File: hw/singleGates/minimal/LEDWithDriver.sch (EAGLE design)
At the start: 8 parts, among them Q1 BC817, Q2 BC817, Q3 BC817

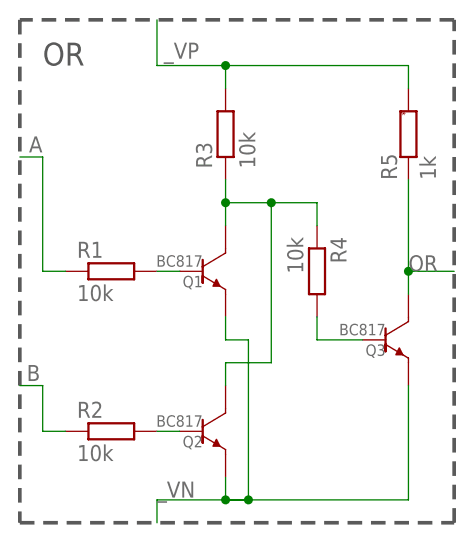
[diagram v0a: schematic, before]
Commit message: Add led output and prepare first alu slice
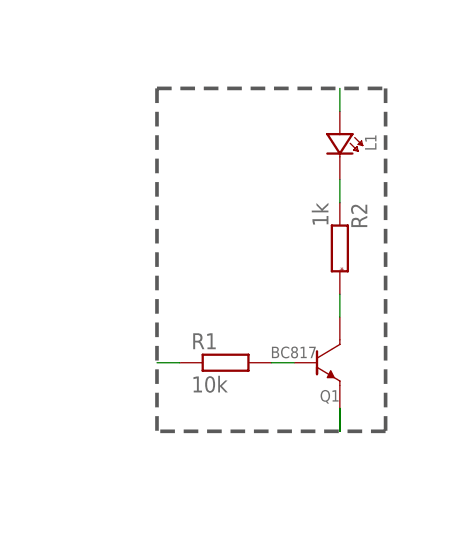
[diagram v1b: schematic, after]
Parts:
- removed Q2, Q3: BC817, p.peter-gator:TRANSISTOR-NPN-GENERICDEFAULT-SOT23-BEC
- removed R3, R4: 10k, p.peter-gator:R-EU_R0603
- removed R5: 1k, p.peter-rcl:R-EU-MARKEDR0603
- added L1: (no value), p.peter-leds:LED0603
- R2: value 10k -> 1k; device p.peter-gator:R-EU_R0603 -> p.peter-rcl:R-EU-MARKEDR0603
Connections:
- removed net B: R2.1
- removed net N$10: Q3.BASE, R4.2
- removed net N$11: Q1.COLLECTOR, Q2.COLLECTOR, R3.1, R4.1
- removed net N$9: Q2.BASE, R2.2
- removed net OR: Q3.COLLECTOR, R5.1
- new net INT: L1.C, R2.1
- new net N$1: Q1.COLLECTOR, R2.2
- net _VN: no longer Q2.EMITTER, Q3.EMITTER
- net _VP: now also L1.A; no longer R3.2, R5.2
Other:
- note removed: "OR"
- moved on the sheet: Q1, R1
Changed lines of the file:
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@@
 <parts>
 <part name="R1" library="p.peter-gator" deviceset="R-EU_" device="R0603" value="10k"/>
-<part name="R2" library="p.peter-gator" deviceset="R-EU_" device="R0603" value="10k"/>
-<part name="R3" library="p.peter-gator" deviceset="R-EU_" device="R0603" value="10k"/>
-<part name="R4" library="p.peter-gator" deviceset="R-EU_" device="R0603" value="10k"/>
-<part name="R5" library="p.peter-rcl" deviceset="R-EU-MARKED" device="R0603" value="1k"/>
+<part name="R2" library="p.peter-rcl" deviceset="R-EU-MARKED" device="R0603" value="1k"/>
 <part name="Q1" library="p.peter-gator" deviceset="TRANSISTOR-NPN-GENERIC" device="-SOT23-BEC" technology="DEFAULT" value="BC817"/>
-<part name="Q2" library="p.peter-gator" deviceset="TRANSISTOR-NPN-GENERIC" device="-SOT23-BEC" technology="DEFAULT" value="BC817"/>
-<part name="Q3" library="p.peter-gator" deviceset="TRANSISTOR-NPN-GENERIC" device="-SOT23-BEC" technology="DEFAULT" value="BC817"/>
+<part name="L1" library="p.peter-leds" deviceset="LED" device="0603"/>
 </parts>
 <sheets>
 <sheet>
 <plain>
-<wire x1="20.32" y1="-27.94" x2="20.32" y2="27.94" width="0.4064" layer="97" style="longdash"/>
-<wire x1="20.32" y1="27.94" x2="-27.94" y2="27.94" width="0.4064" layer="97" style="longdash"/>
-<wire x1="-27.94" y1="27.94" x2="-27.94" y2="-27.94" width="0.4064" layer="97" style="longdash"/>
-<wire x1="-27.94" y1="-27.94" x2="20.32" y2="-27.94" width="0.4064" layer="97" style="longdash"/>
-<text x="-25.4" y="22.86" size="2.54" layer="97" ratio="12">OR</text>
+<wire x1="12.7" y1="-17.78" x2="-12.7" y2="-17.78" width="0.4064" layer="97" style="longdash"/>
+<wire x1="-12.7" y1="20.32" x2="-12.7" y2="-17.78" width="0.4064" layer="97" style="longdash"/>
+<wire x1="12.7" y1="20.32" x2="12.7" y2="-17.78" width="0.4064" layer="97" style="longdash"/>
+<wire x1="-12.7" y1="20.32" x2="12.7" y2="20.32" width="0.4064" layer="97" style="longdash"/>
 </plain>
 <instances>
-<instance part="R1" gate="G$1" x="-17.78" y="0"/>
-<instance part="R2" gate="G$1" x="-17.78" y="-17.78"/>
-<instance part="R3" gate="G$1" x="-5.08" y="15.24" rot="R90"/>
-<instance part="R4" gate="G$1" x="5.08" y="0" rot="R270"/>
-<instance part="R5" gate="G$1" x="15.24" y="15.24" rot="R90"/>
-<instance part="Q1" gate="G$1" x="-5.08" y="0" smashed="yes">
-<attribute name="NAME" x="-7.62" y="-1.778" size="1.27" layer="95" ratio="12" rot="R180" align="top-left"/>
-<attribute name="VALUE" x="-7.62" y="1.778" size="1.27" layer="96" ratio="12" rot="R180"/>
+<instance part="R1" gate="G$1" x="-5.08" y="-10.16"/>
+<instance part="R2" gate="G$1" x="7.62" y="2.54" rot="R270"/>
+<instance part="Q1" gate="G$1" x="7.62" y="-10.16" smashed="yes">
+<attribute name="NAME" x="7.62" y="-14.478" size="1.27" layer="95" ratio="12" rot="R180" align="top-left"/>
+<attribute name="VALUE" x="5.08" y="-8.382" size="1.27" layer="96" ratio="12" rot="R180"/>
 </instance>
-<instance part="Q2" gate="G$1" x="-5.08" y="-17.78" smashed="yes">
-<attribute name="NAME" x="-7.62" y="-19.558" size="1.27" layer="95" ratio="12" rot="R180" align="top-left"/>
-<attribute name="VALUE" x="-7.62" y="-16.002" size="1.27" layer="96" ratio="12" rot="R180"/>
-</instance>
-<instance part="Q3" gate="G$1" x="15.24" y="-7.62" smashed="yes">
-<attribute name="NAME" x="12.7" y="-9.398" size="1.27" layer="95" ratio="12" rot="R180" align="top-left"/>
-<attribute name="VALUE" x="12.7" y="-5.842" size="1.27" layer="96" ratio="12" rot="R180"/>
-</instance>
+<instance part="L1" gate="G$1" x="7.62" y="15.24" rot="R270"/>
 </instances>
 <busses>
 </busses>
 <nets>
+<net name="_VN" class="0">
+<segment>
+<wire x1="7.62" y1="-15.24" x2="7.62" y2="-17.78" width="0.1524" layer="91"/>
+<wire x1="7.62" y1="-17.78" x2="7.62" y2="-15.24" width="0.1524" layer="91"/>
+<wire x1="7.62" y1="-15.24" x2="7.62" y2="-17.78" width="0.1524" layer="91"/>
+<pinref part="Q1" gate="G$1" pin="EMITTER"/>
+</segment>
+</net>
+<net name="N$16" class="0">
+<segment>
+<pinref part="R1" gate="G$1" pin="2"/>
+<wire x1="0" y1="-10.16" x2="2.54" y2="-10.16" width="0.1524" layer="91"/>
+<pinref part="Q1" gate="G$1" pin="BASE"/>
+</segment>
+</net>
 <net name="A" class="0">
 <segment>
 <pinref part="R1" gate="G$1" pin="1"/>
-<wire x1="-22.86" y1="0" x2="-25.4" y2="0" width="0.1524" layer="91"/>
-<wire x1="-25.4" y1="0" x2="-25.4" y2="12.7" width="0.1524" layer="91"/>
-<wire x1="-25.4" y1="12.7" x2="-27.94" y2="12.7" width="0.1524" layer="91"/>
-<label x="-26.924" y="13.208" size="1.778" layer="95"/>
+<wire x1="-10.16" y1="-10.16" x2="-12.7" y2="-10.16" width="0.1524" layer="91"/>
 </segment>
 </net>
-<net name="B" class="0">
+<net name="INT" class="0">
 <segment>
 <pinref part="R2" gate="G$1" pin="1"/>
-<wire x1="-22.86" y1="-17.78" x2="-25.4" y2="-17.78" width="0.1524" layer="91"/>
-<wire x1="-25.4" y1="-17.78" x2="-25.4" y2="-12.7" width="0.1524" layer="91"/>
-<wire x1="-25.4" y1="-12.7" x2="-27.94" y2="-12.7" width="0.1524" layer="91"/>
-<label x="-27.178" y="-12.192" size="1.778" layer="95"/>
+<wire x1="7.62" y1="7.62" x2="7.62" y2="10.16" width="0.1524" layer="91"/>
+<pinref part="L1" gate="G$1" pin="C"/>
 </segment>
 </net>
-<net name="OR" class="0">
+<net name="N$1" class="0">
 <segment>
-<wire x1="15.24" y1="-2.54" x2="15.24" y2="0" width="0.1524" layer="91"/>
-<pinref part="R5" gate="G$1" pin="1"/>
-<wire x1="15.24" y1="0" x2="15.24" y2="10.16" width="0.1524" layer="91"/>
-<wire x1="15.24" y1="0" x2="20.32" y2="0" width="0.1524" layer="91"/>
-<junction x="15.24" y="0"/>
-<pinref part="Q3" gate="G$1" pin="COLLECTOR"/>
-<label x="15.24" y="0" size="1.778" layer="95"/>
-</segment>
-</net>
-<net name="_VN" class="0">
-<segment>
-<wire x1="-5.08" y1="-25.4" x2="-5.08" y2="-22.86" width="0.1524" layer="91"/>
-<wire x1="-5.08" y1="-5.08" x2="-5.08" y2="-7.62" width="0.1524" layer="91"/>
-<wire x1="-5.08" y1="-7.62" x2="-2.54" y2="-7.62" width="0.1524" layer="91"/>
-<wire x1="-2.54" y1="-7.62" x2="-2.54" y2="-25.4" width="0.1524" layer="91"/>
-<junction x="-2.54" y="-25.4"/>
-<pinref part="Q1" gate="G$1" pin="EMITTER"/>
-<pinref part="Q2" gate="G$1" pin="EMITTER"/>
-<pinref part="Q3" gate="G$1" pin="EMITTER"/>
-<wire x1="15.24" y1="-25.4" x2="15.24" y2="-12.7" width="0.1524" layer="91"/>
-<wire x1="-2.54" y1="-25.4" x2="-5.08" y2="-25.4" width="0.1524" layer="91"/>
-<label x="-12.7" y="-25.146" size="1.778" layer="95"/>
-<wire x1="-12.7" y1="-25.4" x2="-5.08" y2="-25.4" width="0.1524" layer="91"/>
-<wire x1="-5.08" y1="-25.4" x2="-2.54" y2="-25.4" width="0.1524" layer="91"/>
-<wire x1="-2.54" y1="-25.4" x2="15.24" y2="-25.4" width="0.1524" layer="91"/>
-<wire x1="-12.7" y1="-25.4" x2="-12.7" y2="-27.94" width="0.1524" layer="91"/>
-<junction x="-5.08" y="-25.4"/>
+<pinref part="R2" gate="G$1" pin="2"/>
+<wire x1="7.62" y1="-5.08" x2="7.62" y2="-2.54" width="0.1524" layer="91"/>
+<pinref part="Q1" gate="G$1" pin="COLLECTOR"/>
 </segment>
 </net>
 <net name="_VP" class="0">
 <segment>
-<pinref part="R3" gate="G$1" pin="2"/>
-<pinref part="R5" gate="G$1" pin="2"/>
-<wire x1="-5.08" y1="22.86" x2="-5.08" y2="20.32" width="0.1524" layer="91"/>
-<wire x1="15.24" y1="22.86" x2="15.24" y2="20.32" width="0.1524" layer="91"/>
-<wire x1="-12.7" y1="22.86" x2="-5.08" y2="22.86" width="0.1524" layer="91"/>
-<wire x1="-5.08" y1="22.86" x2="15.24" y2="22.86" width="0.1524" layer="91"/>
-<wire x1="-12.7" y1="22.86" x2="-12.7" y2="27.94" width="0.1524" layer="91"/>
-<label x="-11.938" y="23.622" size="1.778" layer="95"/>
-<junction x="-5.08" y="22.86"/>
+<pinref part="L1" gate="G$1" pin="A"/>
+<wire x1="7.62" y1="17.78" x2="7.62" y2="20.32" width="0.1524" layer="91"/>
 </segment>
 </net>
-<net name="N$7" class="0">
-<segment>
-<pinref part="R1" gate="G$1" pin="2"/>
-<wire x1="-12.7" y1="0" x2="-10.16" y2="0" width="0.1524" layer="91"/>
-<pinref part="Q1" gate="G$1" pin="BASE"/>
-</segment>
-</net>
-<net name="N$9" class="0">
-<segment>
-<pinref part="R2" gate="G$1" pin="2"/>
-<wire x1="-10.16" y1="-17.78" x2="-12.7" y2="-17.78" width="0.1524" layer="91"/>
-<pinref part="Q2" gate="G$1" pin="BASE"/>
-</segment>
-</net>
-<net name="N$10" class="0">
-<segment>
-<pinref part="R4" gate="G$1" pin="2"/>
-<wire x1="10.16" y1="-7.62" x2="5.08" y2="-7.62" width="0.1524" layer="91"/>
-<wire x1="5.08" y1="-7.62" x2="5.08" y2="-5.08" width="0.1524" layer="91"/>
-<pinref part="Q3" gate="G$1" pin="BASE"/>
-</segment>
-</net>
-<net name="N$11" class="0">
-<segment>
-<pinref part="R3" gate="G$1" pin="1"/>
-<wire x1="-5.08" y1="10.16" x2="-5.08" y2="7.62" width="0.1524" layer="91"/>
-<wire x1="-5.08" y1="7.62" x2="-5.08" y2="5.08" width="0.1524" layer="91"/>
-<wire x1="0" y1="7.62" x2="-5.08" y2="7.62" width="0.1524" layer="91"/>
-<junction x="-5.08" y="7.62"/>
-<wire x1="-5.08" y1="-10.16" x2="0" y2="-10.16" width="0.1524" layer="91"/>
-<wire x1="-5.08" y1="-12.7" x2="-5.08" y2="-10.16" width="0.1524" layer="91"/>
-<pinref part="R4" gate="G$1" pin="1"/>
-<wire x1="0" y1="7.62" x2="0" y2="-10.16" width="0.1524" layer="91"/>
-<wire x1="5.08" y1="5.08" x2="5.08" y2="7.62" width="0.1524" layer="91"/>
-<wire x1="5.08" y1="7.62" x2="0" y2="7.62" width="0.1524" layer="91"/>
-<junction x="0" y="7.62"/>
-<pinref part="Q1" gate="G$1" pin="COLLECTOR"/>
-<pinref part="Q2" gate="G$1" pin="COLLECTOR"/>
-</segment>
-</net>
